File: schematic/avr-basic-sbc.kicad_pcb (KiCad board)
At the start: 2 copper layers, 94 x 55 mm, 38 parts, among them J1 DC-005 Power Jack, J2 PS/2 keyboard port, J3 RCA Video Jack, J4 Port B, J5 Port A, J6 Port C, J7 Port D, J8 USBasp header, J9 Power output header, U1 ATmega1284P-P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

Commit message: PCB Version v1.1 - AV Video RCA Jack polarity reversed, silkscreen updates
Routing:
- net Net-(J3-Video): track 45.9 -> 46.4 mm
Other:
- board text added: "10/PD2 RX"
- board text added: "11/PD3 TX"
- board text added: "ATMEGA1284P SBC VER 1.1"
- board text added: "OFF"
- board text added: "ON"
- board text added: "OUTPUT ONLY"
- board text removed: "10/PD2"
- board text removed: "11/PD3"
- board text removed: "ATMEGA1284P SBC VER 1.0"
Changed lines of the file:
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@@
         (effects (font (size 0.800724 0.800724) (thickness 0.15)))
     )
-    (fp_line (start -7 -7.32) (end -7 -3.3)
+    (fp_line (start -7 -8.382) (end -7 -3.3)
       (stroke (width 0.127) (type solid)) (layer "F.SilkS"))
     (fp_line (start -7 1.68) (end -7 4.7)
@@
     (fp_line (start -7 4.7) (end 7 4.7)
       (stroke (width 0.127) (type solid)) (layer "F.SilkS"))
-    (fp_line (start 7 -7.32) (end -7 -7.32)
+    (fp_line (start 7 -8.382) (end -7 -8.382)
       (stroke (width 0.127) (type solid)) (layer "F.SilkS"))
-    (fp_line (start 7 -3.3) (end 7 -7.32)
+    (fp_line (start 7 -3.3) (end 7 -8.382)
       (stroke (width 0.127) (type solid)) (layer "F.SilkS"))
     (fp_line (start 7 4.7) (end 7 1.68)
@@
     (fp_line (start -8.75 1.25) (end -7.25 1.25)
       (stroke (width 0.05) (type solid)) (layer "F.CrtYd"))
-    (fp_line (start -7.25 -7.57) (end -7.25 -2.75)
+    (fp_line (start -7.25 -8.636) (end -7.25 -2.75)
       (stroke (width 0.05) (type solid)) (layer "F.CrtYd"))
     (fp_line (start -7.25 -2.75) (end -8.75 -2.75)
@@
     (fp_line (start -7.25 5.76) (end 7.25 5.76)
       (stroke (width 0.05) (type solid)) (layer "F.CrtYd"))
-    (fp_line (start 7.25 -7.57) (end -7.25 -7.57)
+    (fp_line (start 7.25 -8.636) (end -7.25 -8.636)
       (stroke (width 0.05) (type solid)) (layer "F.CrtYd"))
-    (fp_line (start 7.25 -2.75) (end 7.25 -7.57)
+    (fp_line (start 7.25 -2.75) (end 7.25 -8.636)
       (stroke (width 0.05) (type solid)) (layer "F.CrtYd"))
     (fp_line (start 7.25 1.25) (end 8.75 1.25)
@@
     (fp_line (start 8.75 1.25) (end 8.75 -2.75)
       (stroke (width 0.05) (type solid)) (layer "F.CrtYd"))
-    (fp_line (start -7 -7.32) (end -7 4.7)
+    (fp_line (start -7 -8.382) (end -7 4.7)
       (stroke (width 0.127) (type solid)) (layer "F.Fab"))
     (fp_line (start -7 4.7) (end -7 5.51)
@@
     (fp_line (start -7 5.51) (end 7 5.51)
       (stroke (width 0.127) (type solid)) (layer "F.Fab"))
-    (fp_line (start 7 -7.32) (end -7 -7.32)
+    (fp_line (start 7 -8.382) (end -7 -8.382)
       (stroke (width 0.127) (type solid)) (layer "F.Fab"))
-    (fp_line (start 7 4.7) (end 7 -7.32)
+    (fp_line (start 7 4.7) (end 7 -8.382)
       (stroke (width 0.127) (type solid)) (layer "F.Fab"))
     (fp_line (start 7 5.51) (end 7 4.7)
@@
     (fp_line (start 10.16 7.62) (end 10.16 -7.62)
       (stroke (width 0.127) (type solid)) (layer "F.Fab"))
-    (pad "1" thru_hole circle (at 5.95 -5 90) (size 3.616 3.616) (drill 2.6) (layers "*.Cu" "*.Mask")
+    (pad "1" thru_hole circle (at 1.45 0 90) (size 3.616 3.616) (drill 2.6) (layers "*.Cu" "*.Mask")
       (net 2 "GND") (pinfunction "Shield") (pintype "passive") (solder_mask_margin 0.102))
-    (pad "1" thru_hole circle (at 5.95 5 90) (size 3.616 3.616) (drill 2.6) (layers "*.Cu" "*.Mask")
-      (net 2 "GND") (pinfunction "Shield") (pintype "passive") (solder_mask_margin 0.102))
-    (pad "2" thru_hole circle (at 1.45 0 90) (size 3.616 3.616) (drill 2.6) (layers "*.Cu" "*.Mask")
+    (pad "2" thru_hole circle (at 5.95 -5 90) (size 3.616 3.616) (drill 2.6) (layers "*.Cu" "*.Mask")
+      (net 58 "Net-(J3-Video)") (pinfunction "Video") (pintype "passive") (solder_mask_margin 0.102))
+    (pad "2" thru_hole circle (at 5.95 5 90) (size 3.616 3.616) (drill 2.6) (layers "*.Cu" "*.Mask")
       (net 58 "Net-(J3-Video)") (pinfunction "Video") (pintype "passive") (solder_mask_margin 0.102))
     (model "${KICAD_USER_3DMODEL_DIR}/CUI_DEVICES_RCJ-044.step"
@@
     )
   )
+  (gr_line (start 151.638 97.9678) (end 152.4 97.9678)
+    (stroke (width 0.15) (type default)) (layer "F.SilkS"))
+  (gr_line (start 152.146 97.7138) (end 152.4 97.9678)
+    (stroke (width 0.15) (type default)) (layer "F.SilkS"))
+  (gr_line (start 152.4 97.9678) (end 152.146 98.2218)
+    (stroke (width 0.15) (type default)) (layer "F.SilkS"))
+  (gr_line (start 151.892 95.6818) (end 151.638 95.4278)
+    (stroke (width 0.15) (type default)) (layer "F.SilkS"))
+  (gr_line (start 151.638 95.4278) (end 151.892 95.1738)
+    (stroke (width 0.15) (type default)) (layer "F.SilkS"))
+  (gr_line (start 152.4 95.4278) (end 151.638 95.4278)
+    (stroke (width 0.15) (type default)) (layer "F.SilkS"))
   (gr_rect (start 91.42 53.34) (end 185.42 108.34)
     (stroke (width 0.1) (type default)) (fill none) (layer "Edge.Cuts"))
@@
     (effects (font (size 1 1) (thickness 0.15)) (justify left bottom))
   )
-  (gr_text "11/PD3" (at 150.241 97.536) (layer "F.SilkS")
+  (gr_text "11/PD3\nTX" (at 150.241 98.298) (layer "F.SilkS")
     (effects (font (size 0.508 0.508) (thickness 0.127)) (justify left bottom))
   )
@@
     (effects (font (size 0.508 0.508) (thickness 0.127)) (justify left bottom))
   )
+  (gr_text "OFF" (at 131.572 72.136) (layer "F.SilkS")
+    (effects (font (size 0.508 0.508) (thickness 0.127)) (justify left bottom))
+  )
   (gr_text "24/A0/PA0" (at 178.943 56.896) (layer "F.SilkS")
     (effects (font (size 0.508 0.508) (thickness 0.127)) (justify left bottom))
@@
     (effects (font (size 1 1) (thickness 0.15)) (justify left bottom))
   )
-  (gr_text "ATMEGA1284P SBC VER 1.0" (at 184.785 98.298 90) (layer "F.SilkS")
+  (gr_text "ATMEGA1284P SBC VER 1.1" (at 184.785 98.298 90) (layer "F.SilkS")
     (effects (font (size 1 1) (thickness 0.15)) (justify left bottom))
   )
@@
     (effects (font (size 0.508 0.508) (thickness 0.127)) (justify left bottom))
   )
+  (gr_text "OUTPUT\nONLY" (at 121.666 62.611 90) (layer "F.SilkS")
+    (effects (font (size 0.508 0.508) (thickness 0.127)) (justify left bottom))
+  )
   (gr_text "22/PC6" (at 178.816 87.376) (layer "F.SilkS")
     (effects (font (size 0.508 0.508) (thickness 0.127)) (justify left bottom))
@@
     (effects (font (size 1 1) (thickness 0.15)) (justify left bottom))
   )
-  (gr_text "14/PD6\nLED" (at 150.241 102.616) (layer "F.SilkS")
+  (gr_text "ON" (at 131.572 78.74) (layer "F.SilkS")
+    (effects (font (size 0.508 0.508) (thickness 0.127)) (justify left bottom))
+  )
+  (gr_text "14/PD6\nLED" (at 150.241 103.378) (layer "F.SilkS")
     (effects (font (size 0.508 0.508) (thickness 0.127)) (justify left bottom))
   )
-  (gr_text "10/PD2" (at 150.241 94.996) (layer "F.SilkS")
+  (gr_text "10/PD2\nRX" (at 150.241 95.758) (layer "F.SilkS")
     (effects (font (size 0.508 0.508) (thickness 0.127)) (justify left bottom))
   )
@@
   (segment (start 141.224 87.249) (end 140.0957 88.3773) (width 0.25) (layer "F.Cu") (net 55))
   (segment (start 140.0957 88.3773) (end 129.5092 88.3773) (width 0.25) (layer "F.Cu") (net 55))
-  (segment (start 142.113 99.695) (end 142.113 104.087) (width 0.25) (layer "F.Cu") (net 58))
+  (segment (start 135.401 99.587) (end 137.113 99.587) (width 0.25) (layer "F.Cu") (net 58))
   (segment (start 120.396 87.884) (end 123.698 87.884) (width 0.25) (layer "F.Cu") (net 58))
-  (segment (start 131.572 95.758) (end 138.176 95.758) (width 0.25) (layer "F.Cu") (net 58))
-  (segment (start 123.698 87.884) (end 131.572 95.758) (width 0.25) (layer "F.Cu") (net 58))
-  (segment (start 138.176 95.758) (end 142.113 99.695) (width 0.25) (layer "F.Cu") (net 58))
   (segment (start 113.284 80.772) (end 120.396 87.884) (width 0.25) (layer "F.Cu") (net 58))
+  (segment (start 123.698 87.884) (end 135.401 99.587) (width 0.25) (layer "F.Cu") (net 58))
   (segment (start 113.284 75.946) (end 113.284 80.772) (width 0.25) (layer "F.Cu") (net 58))
+  (segment (start 137.113 99.587) (end 147.113 99.587) (width 0.25) (layer "F.Cu") (net 58))
   (zone (net 2) (net_name "GND") (layers "F&B.Cu") (hatch edge 0.5)
     (connect_pads (clearance 0.5))

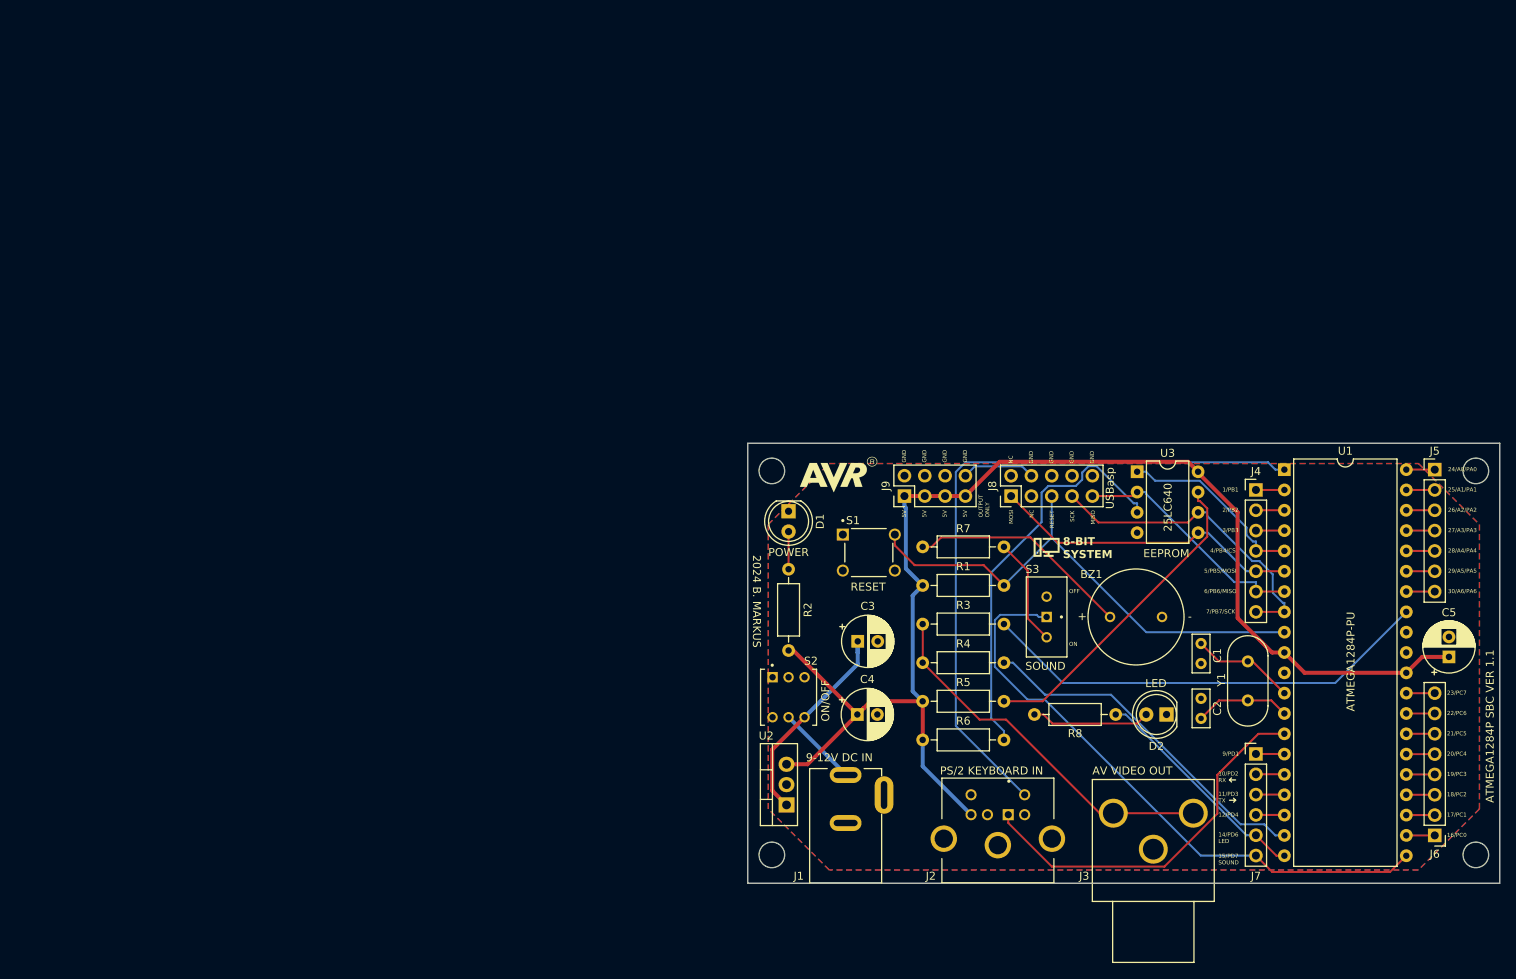
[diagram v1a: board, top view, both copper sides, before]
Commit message: AVR-SBC board updated - USBasp header realigned to match 0.254mm grid
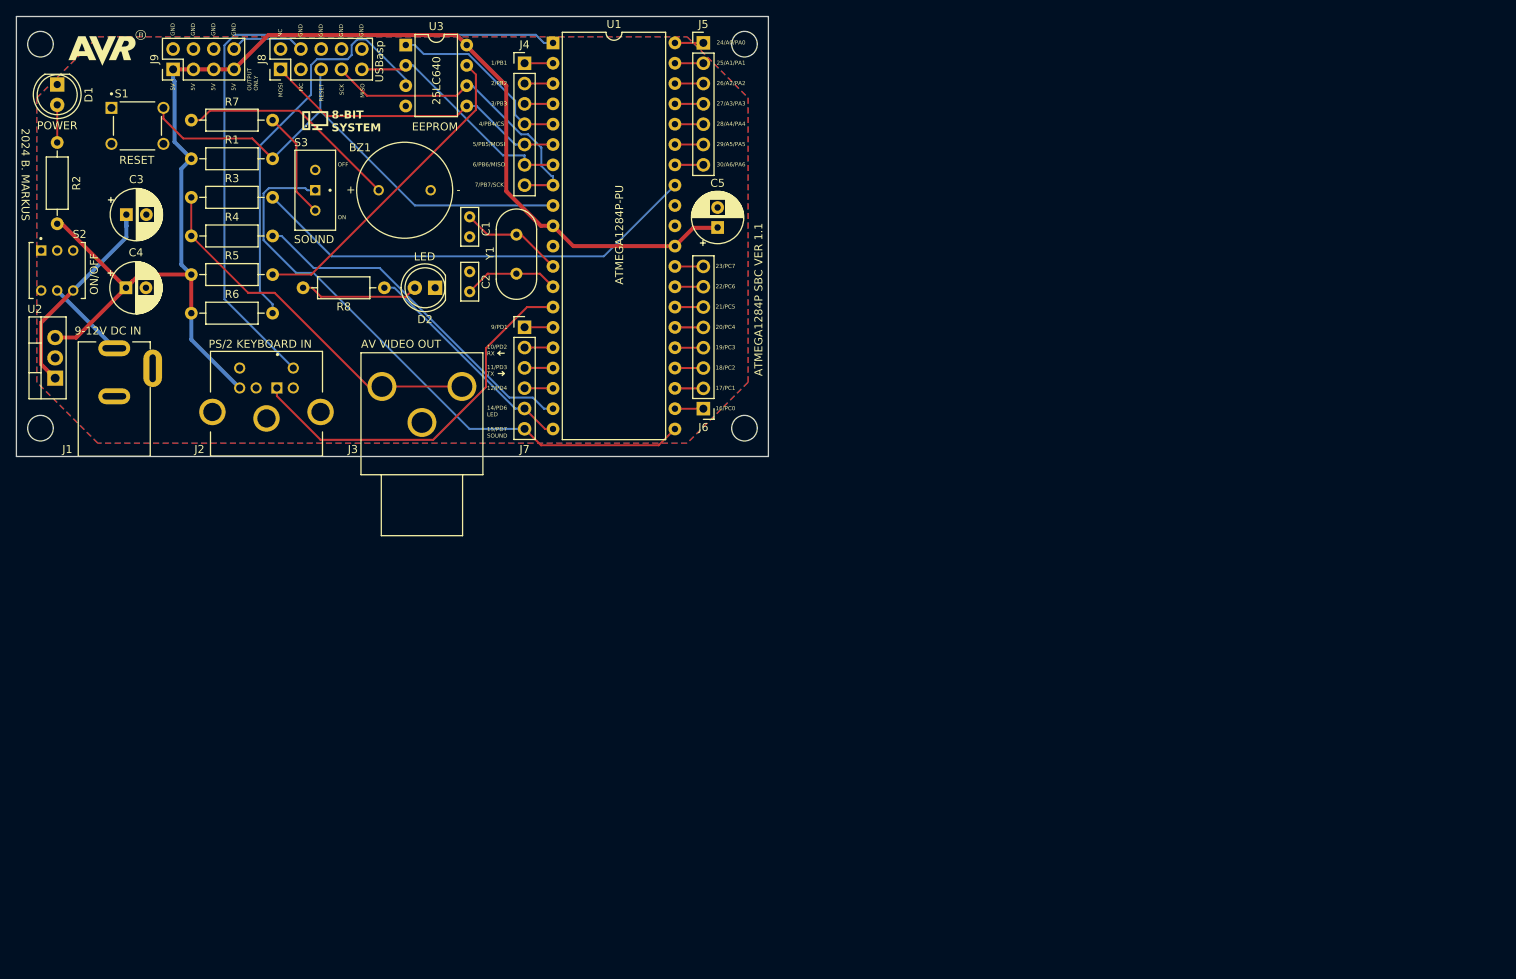
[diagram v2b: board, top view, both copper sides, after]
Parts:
- moved C5 106.0 mm to (87.7, 26.4)
- moved BZ1 105.8 mm to (48.5, 21.7)
- moved D2 105.8 mm to (52.3, 33.9)
- moved U1 105.8 mm to (67.1, 3.30)
- moved U3 105.8 mm to (48.7, 3.57)
- moved Y1 105.8 mm to (62.5, 27.3)
- moved C1 105.8 mm to (56.7, 25.0)
- moved C3 105.8 mm to (13.7, 24.8)
- moved C4 105.8 mm to (13.7, 33.9)
- moved D1 105.8 mm to (5.10, 8.50)
- moved GRAPHICS1 105.8 mm to (11.2, 4.06)
- moved J1 105.8 mm to (12.2, 44.0)
- moved J2 105.8 mm to (31.3, 50.2)
- moved J3 105.8 mm to (50.7, 52.2)
- moved J4 105.8 mm to (63.5, 5.84)
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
